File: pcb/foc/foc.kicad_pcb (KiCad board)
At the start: 2 copper layers, 9 parts, among them J1 PH_2.0, J2 TB_MOTOR, Q1 BTN8982TA, Q2 BTN8982TA, Q3 BTN8982TA, U1 INA240A2PW, U2 INA240A2PW

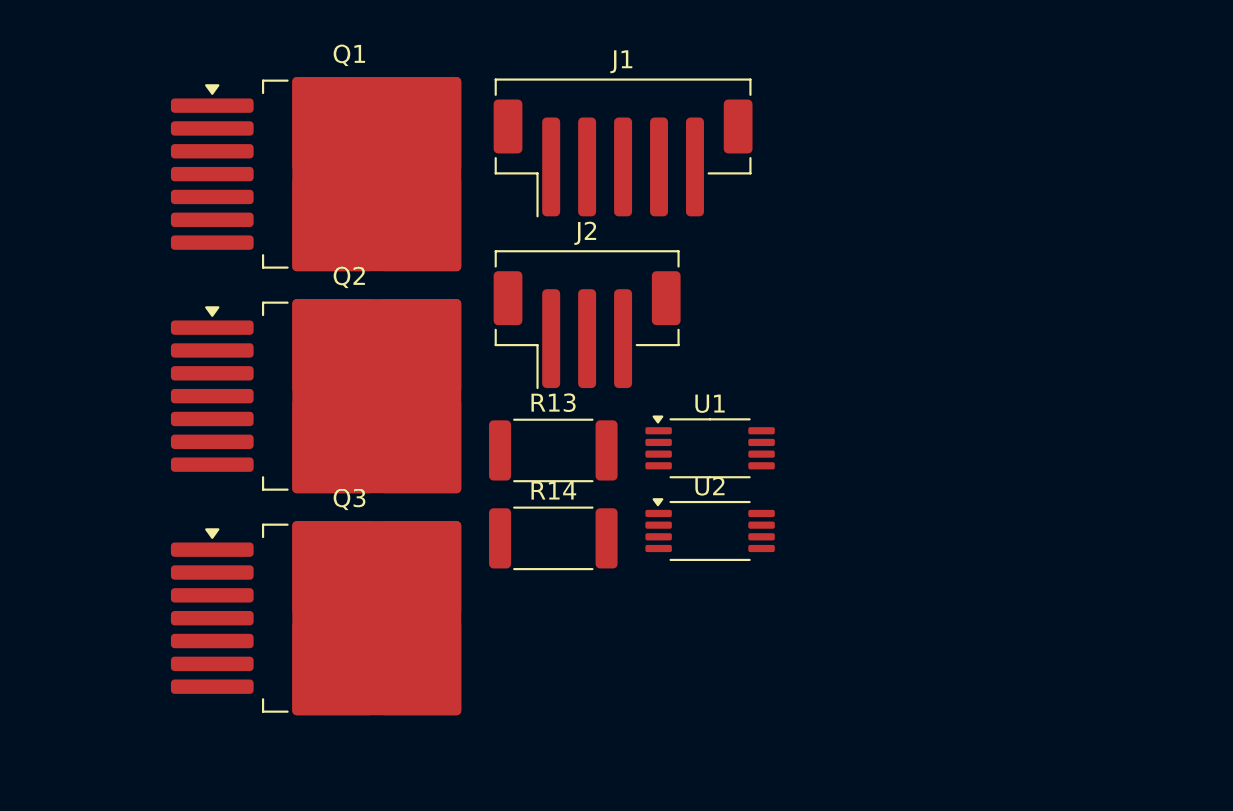
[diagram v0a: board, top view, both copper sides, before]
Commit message: assign foot prints
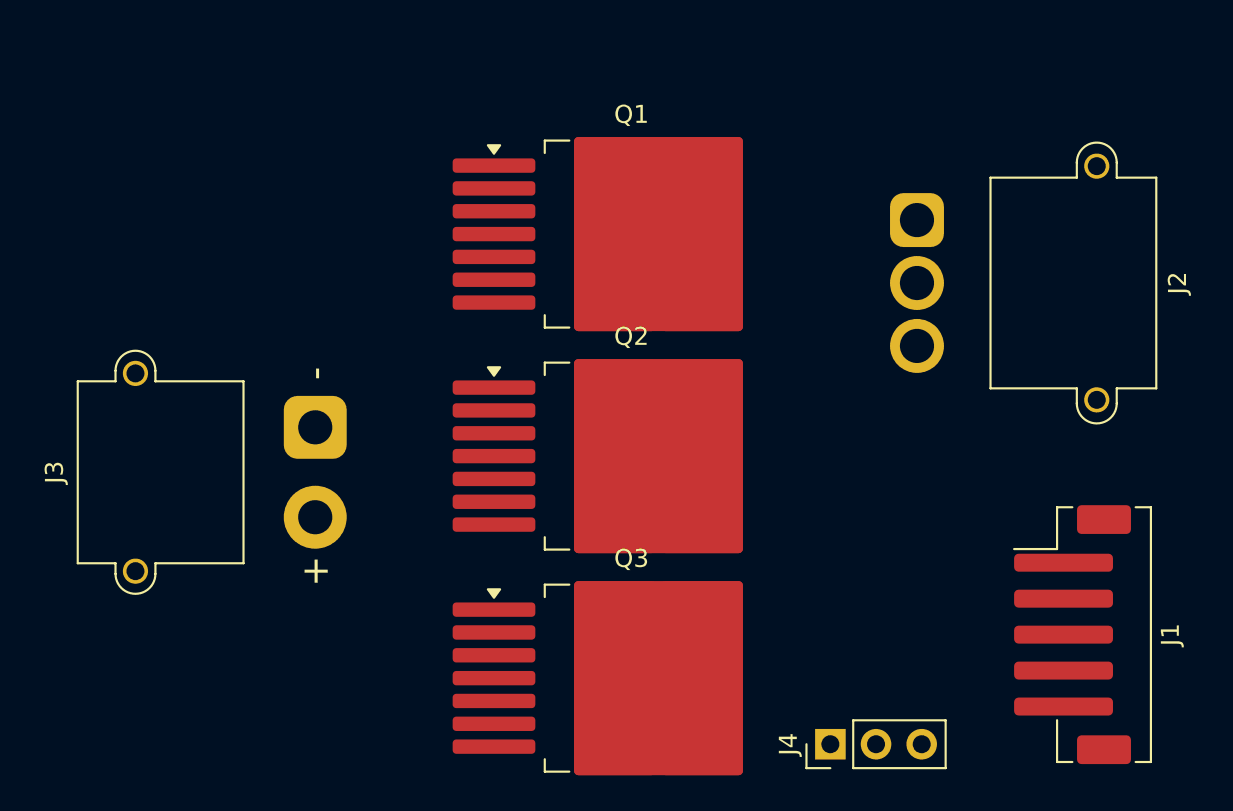
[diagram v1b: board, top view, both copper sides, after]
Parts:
- removed R13, R14: 0.001, Resistor_SMD:R_2512_6332Metric
- removed U1, U2: INA240A2PW, Package_SO:TSSOP-8_4.4x3mm_P0.65mm
- added J3: Power42V, Connector_AMASS:AMASS_XT30PW-M_1x02_P2.50mm_Horizontal, F.Cu at (119.2, 86.3)
- added J4: Conn_01x03_Pin, Connector_PinHeader_2.54mm:PinHeader_1x03_P2.54mm_Vertical, F.Cu at (147.8, 103.9)
- J2: footprint Connector_JST:JST_PH_B3B-PH-SM4-TB_1x03-1MP_P2.00mm_Vertical -> Connector_AMASS:AMASS_MR30PW-M_1x03_P3.50mm_Horizontal
- moved J1 36.4 mm to (161.3, 97.8), turned to -90 degrees
- moved J2 19.3 mm to (152.6, 74.7), turned to -90 degrees
- moved Q1 16.0 mm to (136.8, 75.5)
- moved Q2 16.0 mm to (136.8, 87.9)
- moved Q3 16.0 mm to (136.8, 100.2)

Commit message: 更新原理图和pcb
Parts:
- removed J3: Power42V, Connector_AMASS:AMASS_XT30PW-M_1x02_P2.50mm_Horizontal
- removed J4: Conn_01x03_Pin, Connector_PinHeader_2.54mm:PinHeader_1x03_P2.54mm_Vertical
- added 3.3V1: LED, LED_SMD:LED_0603_1608Metric, F.Cu at (118.0, 91.0)
- added 3.3v0: Power3.3, Connector_PinHeader_2.54mm:PinHeader_1x02_P2.54mm_Vertical, F.Cu at (99.2, 70.5)
- added 42V1: LED, LED_SMD:LED_0603_1608Metric, F.Cu at (118.0, 88.1)
- added 42v0: Power42V, Connector_AMASS:AMASS_XT60PW-M_1x02_P7.20mm_Horizontal, F.Cu at (113.2, 84.6)
- added C1: 100nF, Capacitor_SMD:C_0603_1608Metric, F.Cu at (124.2, 75.0)
- added C10: 20pF, Capacitor_SMD:C_0603_1608Metric, F.Cu at (107.1, 91.9)
- added C11: 100nF, Capacitor_SMD:C_0603_1608Metric, F.Cu at (109.3, 98.8)
- added C12: 20pF, Capacitor_SMD:C_0603_1608Metric, F.Cu at (107.1, 98.8)
- added C13: 100nF, Capacitor_SMD:C_0603_1608Metric, F.Cu at (109.3, 95.2)
- added C14: 20pF, Capacitor_SMD:C_0603_1608Metric, F.Cu at (107.0, 95.3)
- added C2: 1nF, Capacitor_SMD:C_0603_1608Metric, F.Cu at (118.7, 73.6)
- added C3: 1nF, Capacitor_SMD:C_0603_1608Metric, F.Cu at (118.6, 81.6)
- added C4: 100nF, Capacitor_SMD:C_0603_1608Metric, F.Cu at (124.2, 88.0)
- added C5: 1nF, Capacitor_SMD:C_0603_1608Metric, F.Cu at (117.1, 100.0)
- added C6: 100nF, Capacitor_SMD:C_0603_1608Metric, F.Cu at (123.8, 99.8)
- added C7: 0.1nF, Capacitor_SMD:C_0603_1608Metric, F.Cu at (161.8, 73.0)
- added C8: 0.1nF, Capacitor_SMD:C_0603_1608Metric, F.Cu at (159.8, 102.8)
- added C9: 100nF, Capacitor_SMD:C_0603_1608Metric, F.Cu at (109.3, 91.9)
- added NT1: NetTie_2, NetTie:NetTie-2_SMD_Pad2.0mm, F.Cu at (144.0, 103.3)
- added NT1: NetTie_2, NetTie:NetTie-2_SMD_Pad2.0mm, F.Cu at (142.8, 102.0)
- added NT2: NetTie_2, NetTie:NetTie-2_SMD_Pad2.0mm, F.Cu at (151.5, 93.4)
- added NT3: NetTie_2, NetTie:NetTie-2_SMD_Pad2.0mm, F.Cu at (151.6, 82.4)
- added NT4: NetTie_2, NetTie:NetTie-2_SMD_Pad2.0mm, F.Cu at (144.3, 71.1)
- added NT4: NetTie_2, NetTie:NetTie-2_SMD_Pad2.0mm, F.Cu at (143.1, 72.3)
- added R1: 10k, Resistor_SMD:R_0603_1608Metric, F.Cu at (124.2, 73.3)
- added R10: 1k, Resistor_SMD:R_0603_1608Metric, F.Cu at (117.1, 103.0)
- added R11: 10k, Resistor_SMD:R_0603_1608Metric, F.Cu at (123.8, 96.1)
- added R12: 0.51k, Resistor_SMD:R_0603_1608Metric, F.Cu at (123.8, 101.6)
- added R13: 0.001, Resistor_SMD:R_2512_6332Metric, F.Cu at (147.9, 73.8)
- added R14: 0.001, Resistor_SMD:R_2512_6332Metric, F.Cu at (147.8, 100.4)
- added R15: 3.3k, Resistor_SMD:R_0603_1608Metric, F.Cu at (113.1, 92.2)
- added R16: 3.3k, Resistor_SMD:R_0603_1608Metric, F.Cu at (113.1, 94.9)
- added R17: 3.3k, Resistor_SMD:R_0603_1608Metric, F.Cu at (113.0, 98.1)
- added R18: 10k, Resistor_SMD:R_0603_1608Metric, F.Cu at (118.0, 97.0)
- added R2: 10k, Resistor_SMD:R_0603_1608Metric, F.Cu at (124.1, 70.4)
- added R22: 1k, Resistor_SMD:R_0603_1608Metric, F.Cu at (118.0, 95.5)
- added R3: 0.51k, Resistor_SMD:R_0603_1608Metric, F.Cu at (124.2, 76.7)
- added R4: 1k, Resistor_SMD:R_0603_1608Metric, F.Cu at (118.7, 76.7)
- added R5: 10k, Resistor_SMD:R_0603_1608Metric, F.Cu at (124.2, 86.0)
- added R6: 1k, Resistor_SMD:R_0603_1608Metric, F.Cu at (118.6, 84.7)
- added R7: 10k, Resistor_SMD:R_0603_1608Metric, F.Cu at (124.2, 84.1)
- added R8: 0.51k, Resistor_SMD:R_0603_1608Metric, F.Cu at (124.2, 90.0)
- added R9: 10k, Resistor_SMD:R_0603_1608Metric, F.Cu at (123.8, 98.0)
- added U1: INA240A2PW, Package_SO:TSSOP-8_4.4x3mm_P0.65mm, F.Cu at (157.0, 73.0)
- added U2: INA240A2PW, Package_SO:TSSOP-8_4.4x3mm_P0.65mm, F.Cu at (155.0, 102.8)
- added current1: current info, Connector_PinHeader_2.54mm:PinHeader_1x04_P2.54mm_Vertical, F.Cu at (155.8, 98.9)
- added hall1: hall sig, Connector_PinHeader_2.54mm:PinHeader_1x03_P2.54mm_Vertical, F.Cu at (108.2, 103.5)
- added motor1: sig in, Connector_PinHeader_2.54mm:PinHeader_1x06_P2.54mm_Vertical, F.Cu at (106.5, 70.5)
- moved J1 60.3 mm to (101.0, 97.7), turned to 90 degrees
- moved J2 9.69 mm to (151.6, 84.4)
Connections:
- J1 pad 1: VCC -> +3.3V
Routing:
- net +3.3V: track 0.00 -> 163.8 mm, vias 0 -> 3
- net A2: track 0.00 -> 57.4 mm, vias 0 -> 1
- net A3: track 0.00 -> 48.2 mm, vias 0 -> 1
- net D5: track 0.00 -> 34.5 mm, vias 0 -> 1
- net D4: track 0.00 -> 34.3 mm, vias 0 -> 1
- net VCC: track 0.00 -> 30.5 mm, vias 0 -> 9
- net MOT_C: track 0.00 -> 29.8 mm
- net A0: track 0.00 -> 29.8 mm
- net GND: track 0.00 -> 24.4 mm
- net MOT_B: track 0.00 -> 23.4 mm, vias 0 -> 2
- net D6: track 0.00 -> 22.4 mm
- net MOT_A: track 0.00 -> 19.7 mm, vias 0 -> 2
- net D7: track 0.00 -> 18.3 mm
- net Net-(U1-+): track 0.00 -> 14.4 mm
- net Net-(Q3-IS): track 0.00 -> 14.3 mm
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- added copper zone on F.Cu, net GND
- added copper zone on B.Cu, net VCC
- added copper zone on F.Cu, net out2
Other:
- board outline added: 69.1 x 39 mm

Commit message: focV3 update
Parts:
- removed NT1 (x2), NT2, NT3, NT4 (x2): NetTie_2, NetTie:NetTie-2_SMD_Pad2.0mm
- added C15: 330uf, Capacitor_SMD:CP_Elec_10x10.5, F.Cu at (107.6, 92.8)
- hall1: value hall sig -> sig
- motor1: value sig in -> input; footprint Connector_PinHeader_2.54mm:PinHeader_1x06_P2.54mm_Vertical -> Connector_PinHeader_2.54mm:PinHeader_1x03_P2.54mm_Vertical
- moved J1 59.4 mm to (160.4, 96.2), turned to -90 degrees
- moved current1 54.4 mm to (149.5, 44.8), turned to 0 degrees
- moved C11 51.2 mm to (120.7, 48.9), turned to 0 degrees
- moved C9 49.4 mm to (120.7, 43.8), turned to 0 degrees
- moved hall1 49.3 mm to (125.0, 57.2), turned to 0 degrees
- moved C12 49.3 mm to (120.7, 51.4), turned to 0 degrees
- moved C10 47.5 mm to (120.7, 46.4), turned to 0 degrees
- moved C13 42.9 mm to (120.7, 53.9), turned to 0 degrees
- moved C14 41.3 mm to (120.7, 56.4), turned to 0 degrees
- moved 3.3v0 40.9 mm to (138.0, 57.6), turned to 0 degrees
- moved R17 35.0 mm to (120.7, 63.9), turned to 0 degrees
- moved R16 34.3 mm to (120.7, 61.4), turned to 0 degrees
- moved R15 34.1 mm to (120.7, 58.9), turned to 0 degrees
- moved motor1 26.8 mm to (129.7, 57.2), turned to 0 degrees
- moved 42V1 23.7 mm to (112.9, 111.2)
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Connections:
- R1 pad 2: D9 -> INH_1
- R11 pad 2: D4 -> IN_3
- R13 pad 1: Net-(U1-+) -> out1
- R13 pad 2: Net-(U1--) -> out1_cs
- R14 pad 1: Net-(U2-+) -> out3_cs
- R14 pad 2: Net-(U2--) -> out3
- R2 pad 2: D8 -> IN_1
- R5 pad 2: D6 -> INH_2
- R7 pad 2: D7 -> IN_2
- R9 pad 2: D5 -> INH_3
- U1 pad 2: Net-(U1-+) -> out1
- U1 pad 3: Net-(U1--) -> out1_cs
- U2 pad 2: Net-(U2-+) -> out3_cs
- U2 pad 3: Net-(U2--) -> out3
- motor1 pad 1: D4 -> IN_1
- motor1 pad 2: D5 -> IN_2
- motor1 pad 3: D6 -> IN_3
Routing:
- net +3.3V: track 163.8 -> 4.14 mm, vias 3 -> 0
- net A2: track 57.4 -> 0.00 mm, vias 1 -> 0
- net A3: track 48.2 -> 0.00 mm, vias 1 -> 0
- net D5: track 34.5 -> 0.00 mm, vias 1 -> 0
- net D4: track 34.3 -> 0.00 mm, vias 1 -> 0
- net MOT_C: track 29.8 -> 0.00 mm
- net A0: track 29.8 -> 0.00 mm
- net MOT_B: track 23.4 -> 0.00 mm, vias 2 -> 0
- net D6: track 22.4 -> 0.00 mm
- net VCC: track 30.5 -> 8.55 mm, vias 9 -> 0
- net MOT_A: track 19.7 -> 0.00 mm, vias 2 -> 0
- net D7: track 18.3 -> 0.00 mm
- net GND: track 24.4 -> 8.99 mm
- net Net-(U1-+): track 14.4 -> 0.00 mm
- net Net-(Q3-IS): track 14.3 -> 0.00 mm
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- removed copper zone on F.Cu, net GND
- removed copper zone on B.Cu, net VCC
- removed copper zone on F.Cu, net out2

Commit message: update pcb
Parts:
- added C16: 330uf, Capacitor_SMD:CP_Elec_10x10.5, F.Cu at (104.0, 104.2)
- added motor_en1: en_sig, Connector_PinHeader_2.54mm:PinHeader_1x02_P2.54mm_Vertical, F.Cu at (153.2, 103.8)
- moved current1 63.6 mm to (153.4, 108.3), turned to 90 degrees
- moved C9 61.4 mm to (152.2, 96.5), turned to -90 degrees
- moved C10 60.3 mm to (154.1, 96.5), turned to 90 degrees
- moved 3.3v0 54.5 mm to (118.1, 108.3), turned to -90 degrees
- moved hall1 52.7 mm to (137.9, 108.3), turned to 90 degrees
- moved C11 51.8 mm to (152.2, 90.0), turned to 90 degrees
- moved motor1 51.2 mm to (126.8, 108.3), turned to 90 degrees
- moved C12 51.0 mm to (154.1, 89.9), turned to -90 degrees
- moved C13 50.4 mm to (152.2, 93.2), turned to 90 degrees
- moved R15 50.2 mm to (149.0, 100.3), turned to -90 degrees
- moved C14 49.8 mm to (154.1, 93.2), turned to -90 degrees
- moved R16 45.5 mm to (149.0, 97.0), turned to -90 degrees
- moved R17 41.1 mm to (149.0, 93.7), turned to -90 degrees
- moved 3.3V1 21.8 mm to (113.8, 89.9)
- moved R22 21.1 mm to (113.8, 93.5)
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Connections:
- R1 pad 2: INH_1 -> INH_EN
- R5 pad 2: INH_2 -> INH_EN
- R9 pad 2: INH_3 -> INH_EN
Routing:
- net +3.3V: track 4.14 -> 121.6 mm, vias 0 -> 2
- net INH_EN: track 0.00 -> 78.5 mm, vias 0 -> 7
- net IN_1: track 0.00 -> 78.0 mm, vias 0 -> 1
- net A2: track 0.00 -> 54.5 mm, vias 0 -> 1
- net A3: track 0.00 -> 50.1 mm, vias 0 -> 1
- net IN_2: track 0.00 -> 38.1 mm, vias 0 -> 1
- net VCC: track 8.55 -> 46.6 mm, vias 0 -> 10
- net A0: track 0.00 -> 37.5 mm, vias 0 -> 1
- net MOT_A: track 0.00 -> 32.4 mm, vias 0 -> 1
- net MOT_B: track 0.00 -> 28.1 mm, vias 0 -> 1
- net out3: track 0.00 -> 27.3 mm, vias 0 -> 2
- net MOT_C: track 0.00 -> 24.8 mm, vias 0 -> 1
- net GND: track 8.99 -> 33.6 mm, vias 0 -> 15
- net out2: track 9.15 -> 28.9 mm
- net IN_3: track 0.00 -> 18.0 mm, vias 0 -> 1
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- added copper zone on F.Cu, net GND
- added copper zone on B.Cu, net VCC
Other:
- board size 69.1 x 39 mm -> 68.7 x 44 mm
